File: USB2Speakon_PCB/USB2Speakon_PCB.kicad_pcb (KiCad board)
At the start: 4 copper layers, 15 x 27 mm, 51 parts, among them J1 USB_C_Receptacle_USB2.0_16P, J2 Conn_01x04, U1 PCM2912A, U2 TPA2012D2RTJR, Y1 6 MHz

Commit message: add production files (and some minor tweaks)
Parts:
- moved C2 0.36 mm to (147.7, 87.6)
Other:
- board size 15 x 27 mm -> 15 x 26 mm
- board text added: "L -+"
- board text added: "R +-"

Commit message: some minor changes, idk
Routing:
- net GND: track 51.2 -> 49.9 mm

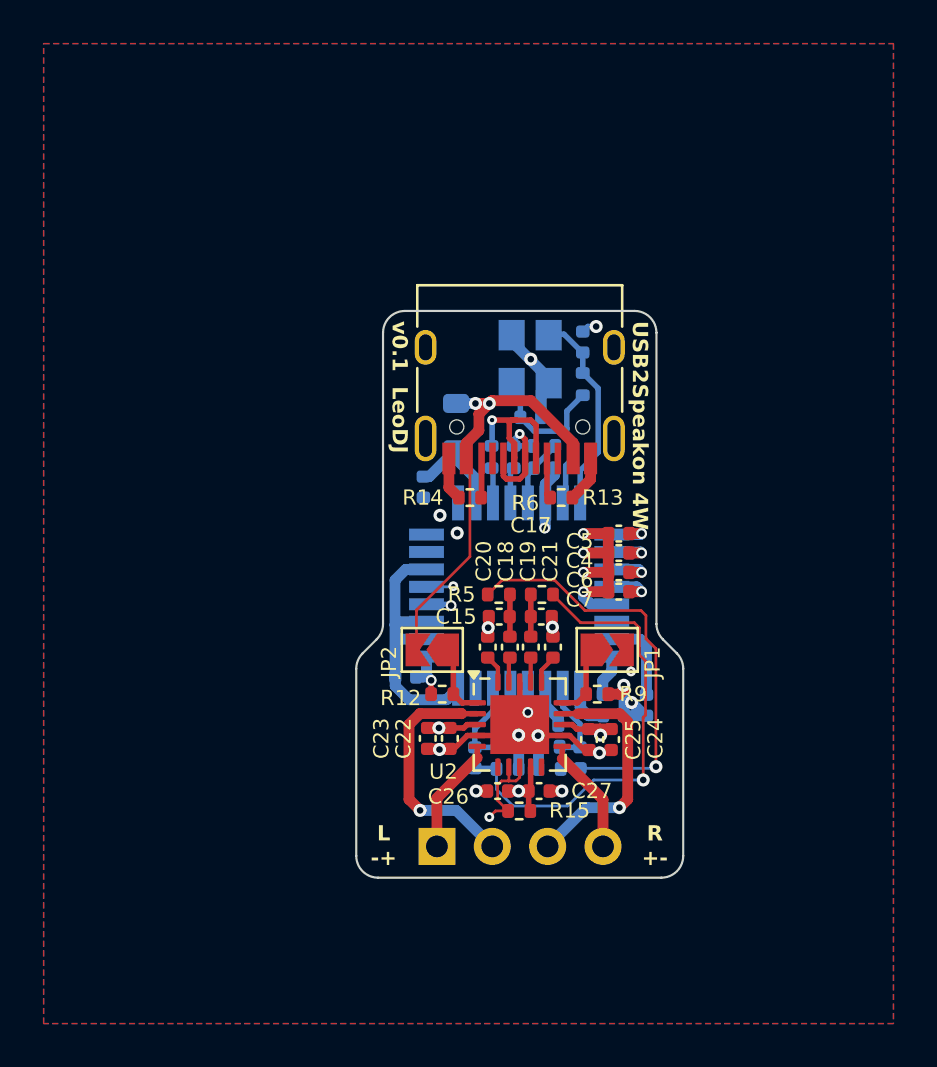
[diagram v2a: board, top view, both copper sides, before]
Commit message: replace crystal with oscillator and add solder pads for a capacitor
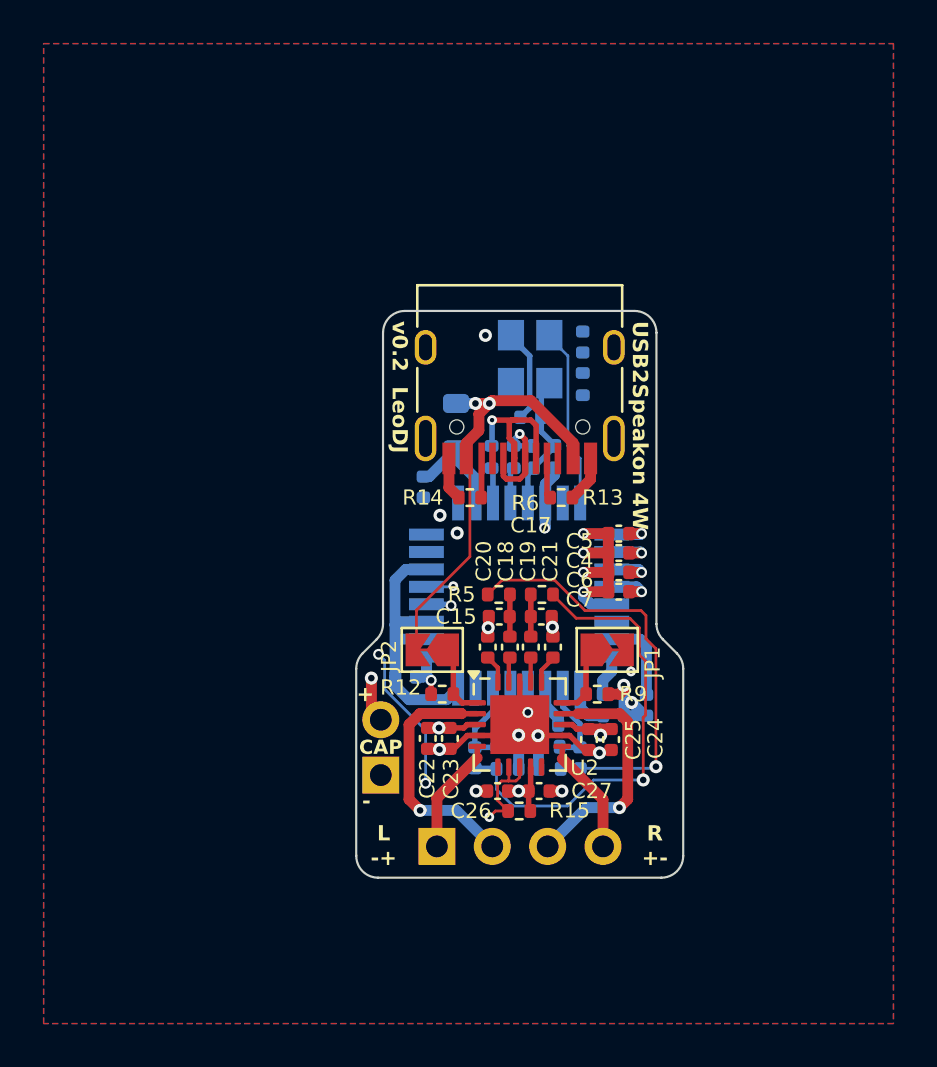
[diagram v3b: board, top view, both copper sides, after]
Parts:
- removed C3: 8p, Capacitor_SMD:C_0402_1005Metric
- removed Y1: 6 MHz, Crystal:Crystal_SMD_3225-4Pin_3.2x2.5mm
- added C29: 100n, Capacitor_SMD:C_0402_1005Metric, B.Cu at (145.3, 91.0)
- added J3: Ext_Cap, Connector_PinSocket_2.54mm:PinSocket_1x02_P2.54mm_Vertical, F.Cu at (138.4, 107.4)
- added X1: 6MHz XO, LCSC:OSC-SMD_4P-L3.2-W2.5-BL, B.Cu at (145.3, 88.4)
- C2: value 8p -> DNP
- R4: value 1M -> DNP
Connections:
- net Net-(U1-VDD) renamed +3V3
- C2 pad 1: GND -> unconnected-(C2-Pad1)
- C2 pad 2: Net-(U1-XTI) -> unconnected-(C2-Pad2)
- JP1 pad 1: Net-(JP1-A) -> VBUS
- JP2 pad 1: Net-(JP2-A) -> VBUS
- R12 pad 1: Net-(JP2-A) -> VBUS
- R4 pad 1: Net-(U1-XTO) -> unconnected-(R4-Pad1)
- R4 pad 2: Net-(U1-XTI) -> unconnected-(R4-Pad2)
- R9 pad 1: Net-(JP1-A) -> VBUS
- U1 pad 7: Net-(U1-XTO) -> unconnected-(U1-XTO-Pad7)
- U2 pad 1: Net-(JP2-A) -> VBUS
- U2 pad 15: Net-(JP1-A) -> VBUS
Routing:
- net VBUS: track 64.3 -> 80.1 mm, vias 6 -> 7
- net Net-(U1-XTO): track 9.71 -> 0.00 mm
- net Net-(JP2-A): track 3.39 -> 0.00 mm
- net Net-(JP1-A): track 3.39 -> 0.00 mm
- net +3V3: track 3.13 -> 6.43 mm
- net ~{SSPND}: track 19.2 -> 21.0 mm, vias 2 -> 4
- net Net-(U1-XTI): track 9.46 -> 8.28 mm
- net GND: track 49.9 -> 48.8 mm, vias 22 -> 21
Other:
- board text added: "+"
- board text added: "-"
- board text added: "CAP"
- board text added: "v0.2 LeoDJ"
- board text removed: "v0.1 LeoDJ"
